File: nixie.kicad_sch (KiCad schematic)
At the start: 40 parts, among them J1 Barrel_Jack, Q1 2N3906, Q2 Q_NMOS_GDS, U1 HV5222PG-G, U2 MC34063AP, U3 4504, U4 LM7805_TO220, U5 HV5222PG-G

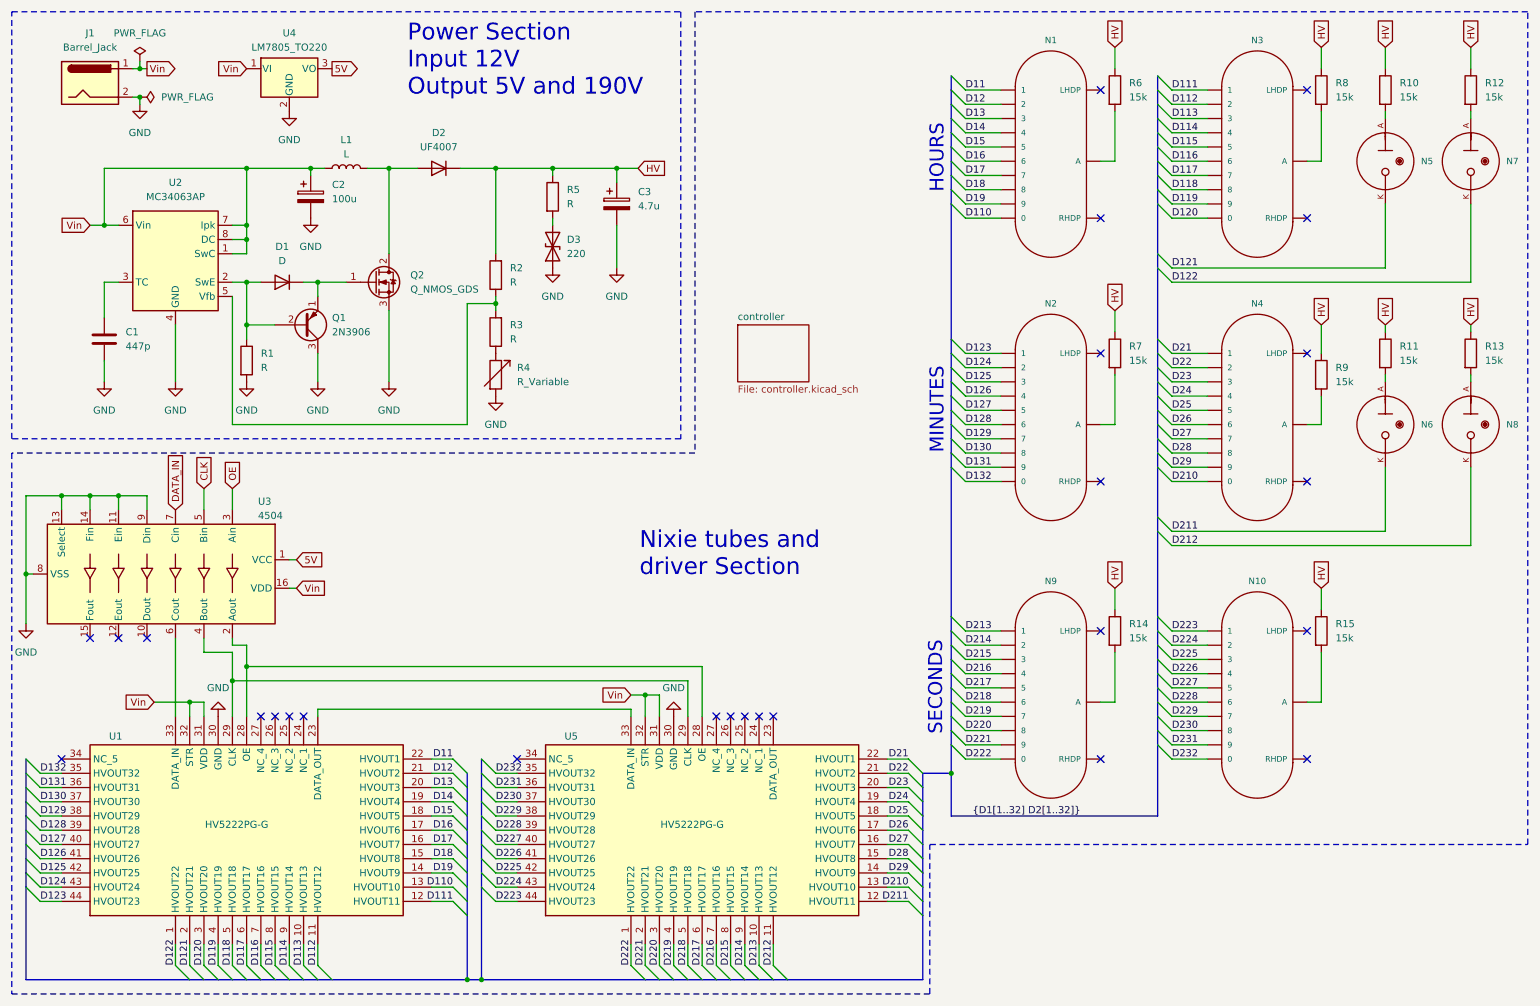
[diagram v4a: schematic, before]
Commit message: added filter caps and rc debounce filter for rotary encoder
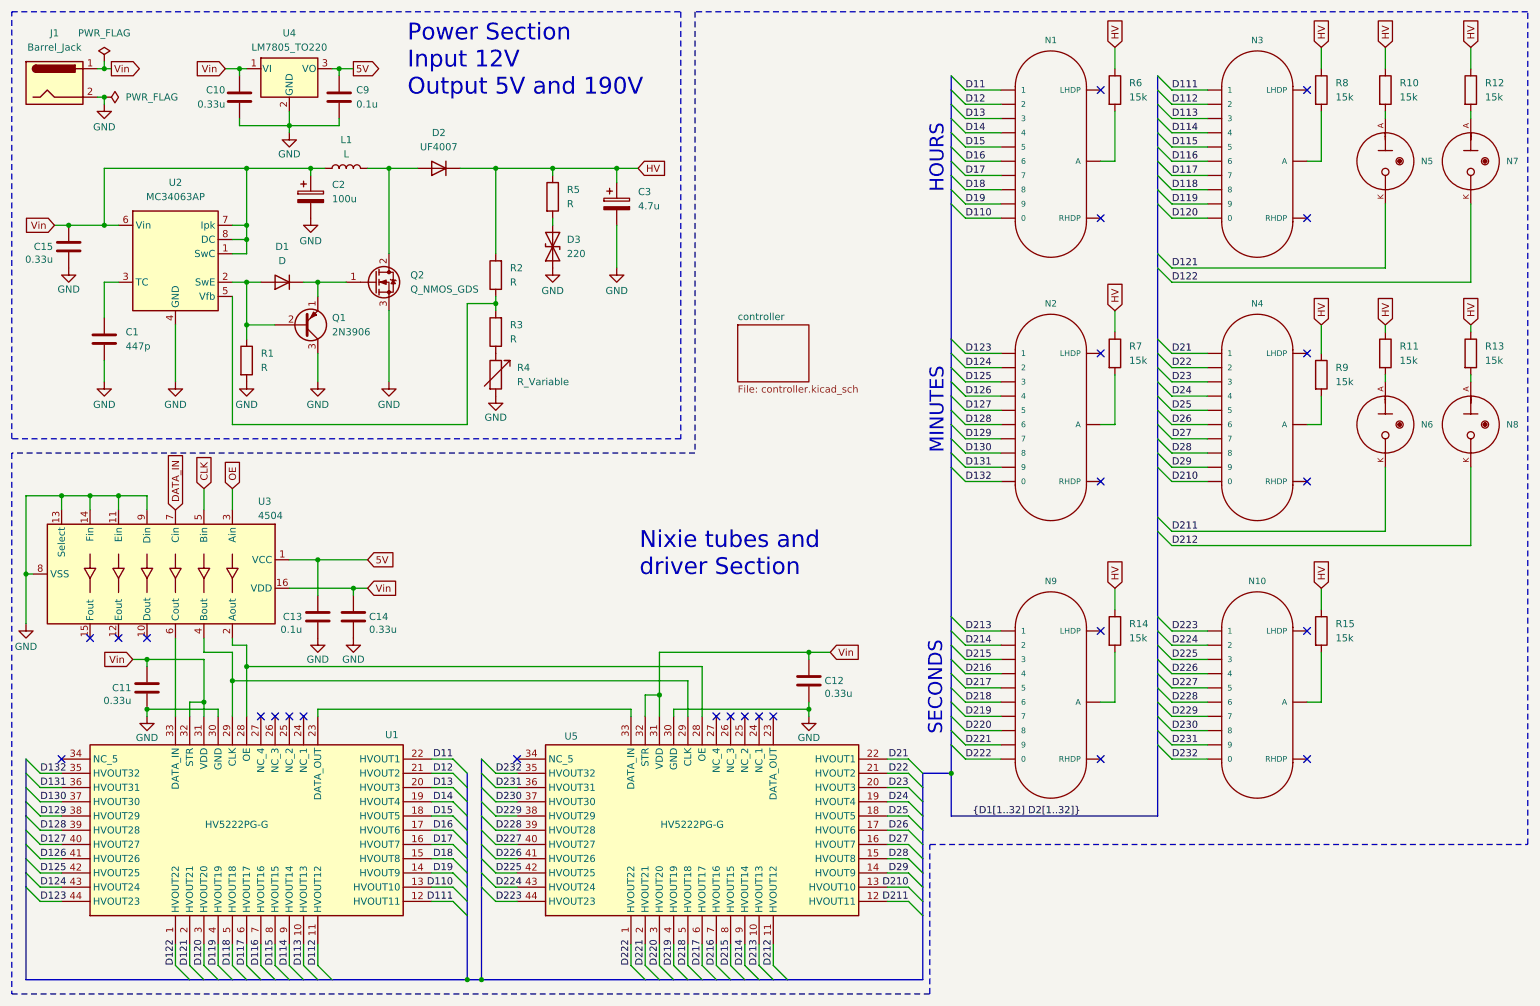
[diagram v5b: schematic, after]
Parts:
- added C10, C11, C12, C14, C15: 0.33u, symbol Device:C
- added C13, C9: 0.1u, symbol Device:C
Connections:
- net 5V: now also C13.1, C9.1
- net GND: now also C10.2, C11.2, C12.2, C13.2, C14.2, C15.2, C9.2
- net Vin: now also C10.1, C11.1, C12.1, C14.1, C15.1
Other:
- moved on the sheet: J1

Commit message: added footprints
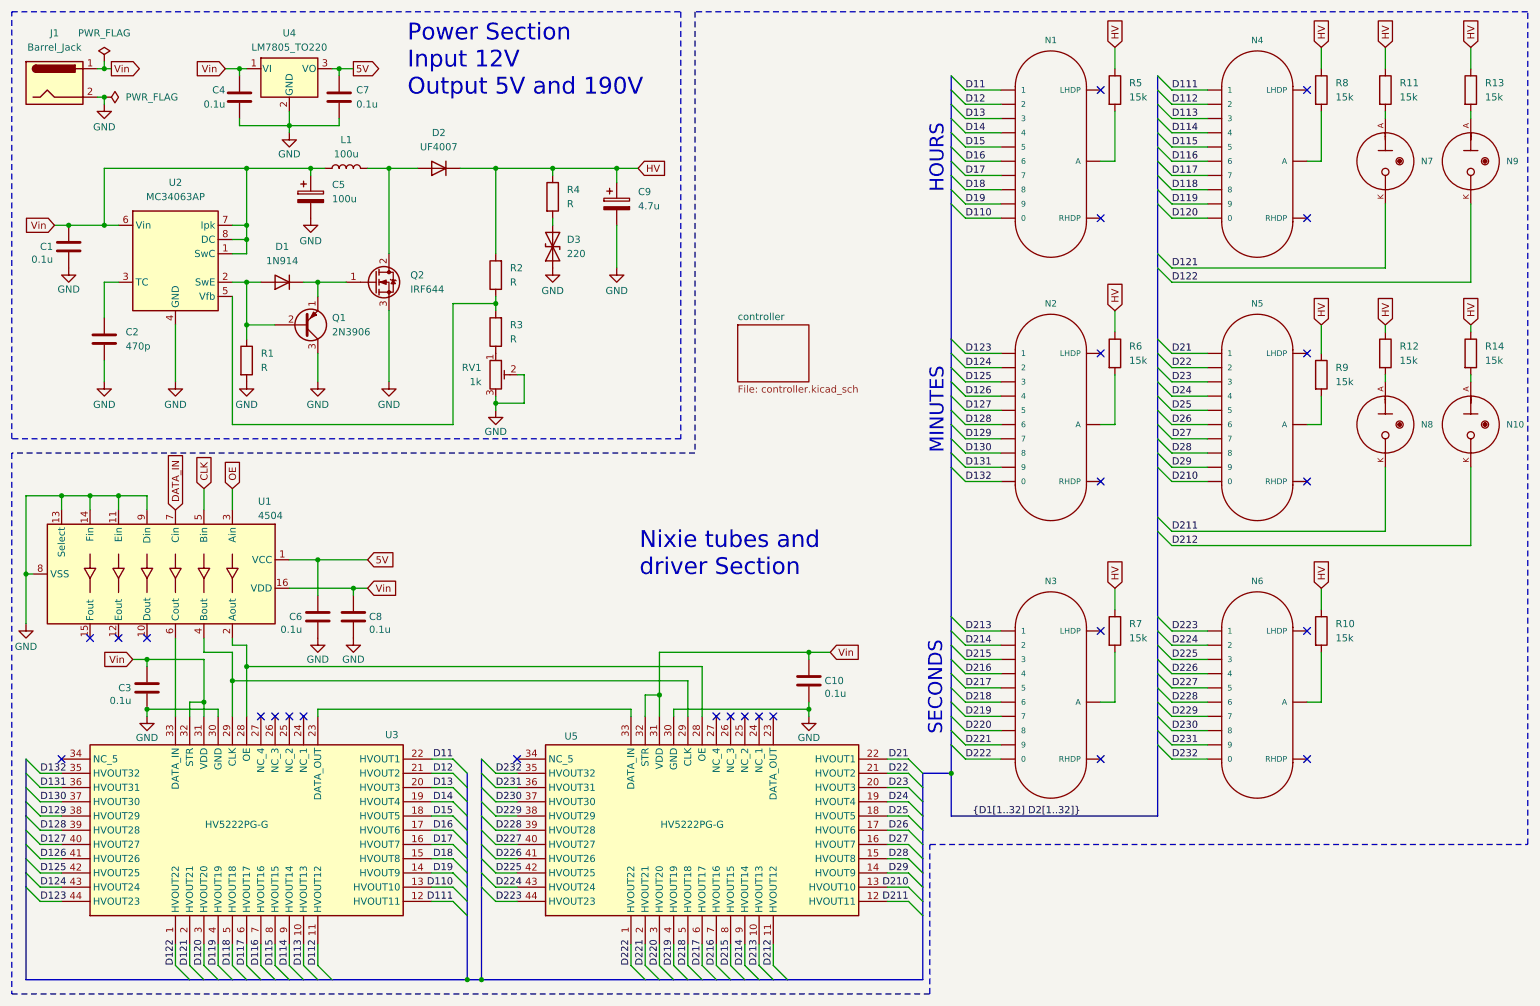
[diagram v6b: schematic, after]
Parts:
- removed D1: D, symbol Device:D
- removed R4: R_Variable, symbol Device:R_Variable
- added D1: 1N914, Diode_THT:D_DO-35_SOD27_P7.62mm_Horizontal, symbol Diode:1N914
- added RV1: 1k, nixie:Potentiometer_Bourns_3306P_Vertical, symbol Device:R_Potentiometer_Trim
- C1: renamed from C15; value 0.33u -> 0.1u; footprint (none) -> Capacitor_THT:C_Disc_D4.7mm_W2.5mm_P5.00mm
- C10: renamed from C12; value 0.33u -> 0.1u; footprint (none) -> Capacitor_THT:C_Disc_D4.7mm_W2.5mm_P5.00mm
- C2: renamed from C1; value 447p -> 470p; footprint (none) -> Capacitor_THT:C_Disc_D3.8mm_W2.6mm_P2.50mm
- C3: renamed from C11; value 0.33u -> 0.1u; footprint (none) -> Capacitor_THT:C_Disc_D4.7mm_W2.5mm_P5.00mm
- C4: renamed from C10; value 0.33u -> 0.1u; footprint (none) -> Capacitor_THT:C_Disc_D4.7mm_W2.5mm_P5.00mm
- C5: renamed from C2; footprint (none) -> Capacitor_THT:CP_Radial_D6.3mm_P2.50mm
- C6: renamed from C13; footprint (none) -> Capacitor_THT:C_Disc_D4.7mm_W2.5mm_P5.00mm
- C7: renamed from C9; footprint (none) -> Capacitor_THT:C_Disc_D4.7mm_W2.5mm_P5.00mm
- C8: renamed from C14; value 0.33u -> 0.1u; footprint (none) -> Capacitor_THT:C_Disc_D4.7mm_W2.5mm_P5.00mm
- C9: renamed from C3; footprint (none) -> Capacitor_THT:CP_Radial_D8.0mm_P3.50mm
- D2: footprint (none) -> Diode_THT:D_DO-41_SOD81_P7.62mm_Horizontal
- D3: footprint (none) -> Diode_THT:D_DO-15_P10.16mm_Horizontal
- J1: footprint (none) -> Connector_BarrelJack:BarrelJack_SwitchcraftConxall_RAPC10U_Horizontal
- L1: value L -> 100u; footprint (none) -> Inductor_THT:L_Radial_D8.7mm_P5.00mm_Fastron_07HCP
- Q2: value Q_NMOS_GDS -> IRF644; footprint (none) -> Package_TO_SOT_THT:TO-220-3_Horizontal_TabDown
- R1, R2, R3, R8, R9: footprint (none) -> Resistor_THT:R_Axial_DIN0207_L6.3mm_D2.5mm_P7.62mm_Horizontal
- R10: renamed from R15; footprint (none) -> Resistor_THT:R_Axial_DIN0207_L6.3mm_D2.5mm_P7.62mm_Horizontal
- R11: renamed from R10; footprint (none) -> Resistor_THT:R_Axial_DIN0207_L6.3mm_D2.5mm_P7.62mm_Horizontal
- R12: renamed from R11; footprint (none) -> Resistor_THT:R_Axial_DIN0207_L6.3mm_D2.5mm_P7.62mm_Horizontal
- R13: renamed from R12; footprint (none) -> Resistor_THT:R_Axial_DIN0207_L6.3mm_D2.5mm_P7.62mm_Horizontal
- R14: renamed from R13; footprint (none) -> Resistor_THT:R_Axial_DIN0207_L6.3mm_D2.5mm_P7.62mm_Horizontal
- R4: renamed from R5; footprint (none) -> Resistor_THT:R_Axial_DIN0207_L6.3mm_D2.5mm_P7.62mm_Horizontal
- R5: renamed from R6; footprint (none) -> Resistor_THT:R_Axial_DIN0207_L6.3mm_D2.5mm_P7.62mm_Horizontal
- R6: renamed from R7; footprint (none) -> Resistor_THT:R_Axial_DIN0207_L6.3mm_D2.5mm_P7.62mm_Horizontal
- R7: renamed from R14; footprint (none) -> Resistor_THT:R_Axial_DIN0207_L6.3mm_D2.5mm_P7.62mm_Horizontal
- renumbered N8 to N10, N9 to N3, N3 to N4, N4 to N5, N10 to N6, N5 to N7, N6 to N8, N7 to N9, U3 to U1, U1 to U3
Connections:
- net GND: now also RV1.2, RV1.3
- net at Q1.1 (E), Q2.1 (G): now also D1.1 (K)
- net at Q1.2 (B), R1.1, U2.2 (SwE): now also D1.2 (A)
- net at R3.1: now also RV1.1

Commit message: first attempt at pcb layout
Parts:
- J1: footprint Connector_BarrelJack:BarrelJack_SwitchcraftConxall_RAPC10U_Horizontal -> Connector_PinHeader_2.54mm:PinHeader_1x02_P2.54mm_Vertical
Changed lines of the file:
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@@
 			)
 		)
-		(property "Footprint" "Connector_BarrelJack:BarrelJack_SwitchcraftConxall_RAPC10U_Horizontal"
+		(property "Footprint" "Connector_PinHeader_2.54mm:PinHeader_1x02_P2.54mm_Vertical"
 			(at 21.59 30.226 0)
 			(effects

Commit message: pcb layout updated
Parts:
- added H1, H2, H3, H4: MountingHole_Pad, MountingHole:MountingHole_3.2mm_M3_Pad_Via, symbol Mechanical:MountingHole_Pad
- U4: footprint Package_TO_SOT_THT:TO-220-3_Vertical -> Package_TO_SOT_THT:TO-220-3_Horizontal_TabDown
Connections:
- net GND: now also H1.1, H2.1, H3.1, H4.1
